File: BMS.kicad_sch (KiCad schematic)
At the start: 89 parts, among them J1 Conn_02x02_Counter_Clockwise, J10 OLED, J2 Conn_02x02_Counter_Clockwise, J3 RJ45, J4 Conn_02x08_Top_Bottom, J5 Conn_02x05_Top_Bottom, J6 Conn_02x02_Counter_Clockwise, J7 Conn_02x02_Counter_Clockwise, J8 Conn_02x08_Top_Bottom, Q1 BSS138LT1G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

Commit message: PCB Improvements - VIAS/Pours UNFINISHED
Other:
- moved on the sheet: BT1, C15, D43, H1, H2, H3, H4, J10, J3, J7, J8, JP1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

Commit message: J5 Bottom Silkscreen, Schematic organise
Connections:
- net Overcurrent_Protection1/V_{OUT} renamed 5V_Out_J4
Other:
- note added: "12v Input Processing"
- note added: "5V Supply"
- note added: "CAN1 ISOLATED (J6)"
- note added: "CAN2 Transceiver (J5)"
- note added: "CAN3 Transceiver (J3)"
- note added: "Connector J1 - Serial ISOLATED"
- note added: "Connector J6 - CAN ISOLATED"
- note added: "RS-485 Transceiver (J7)"
- note added: "Scrap Book"
- note added: "Serial ISOLATED (J1)"
- note added: "UART Buffer (J5)"
- note removed: "CAN Connector ISOLATED"
- note removed: "CAN Transceivers - Non Isolated"
- note removed: "CAN1 ISOLATED"
- note removed: "Power Supply"
- note removed: "RS-485 Interface"
- note removed: "Serial Connector ISOLATED"
- note removed: "Serial ISOLATED"
- note removed: "UART Buffer"
- moved on the sheet: BC1, BC2, BC3, BT1, C11, C12, C13, C14, C15, C16, C17, C18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

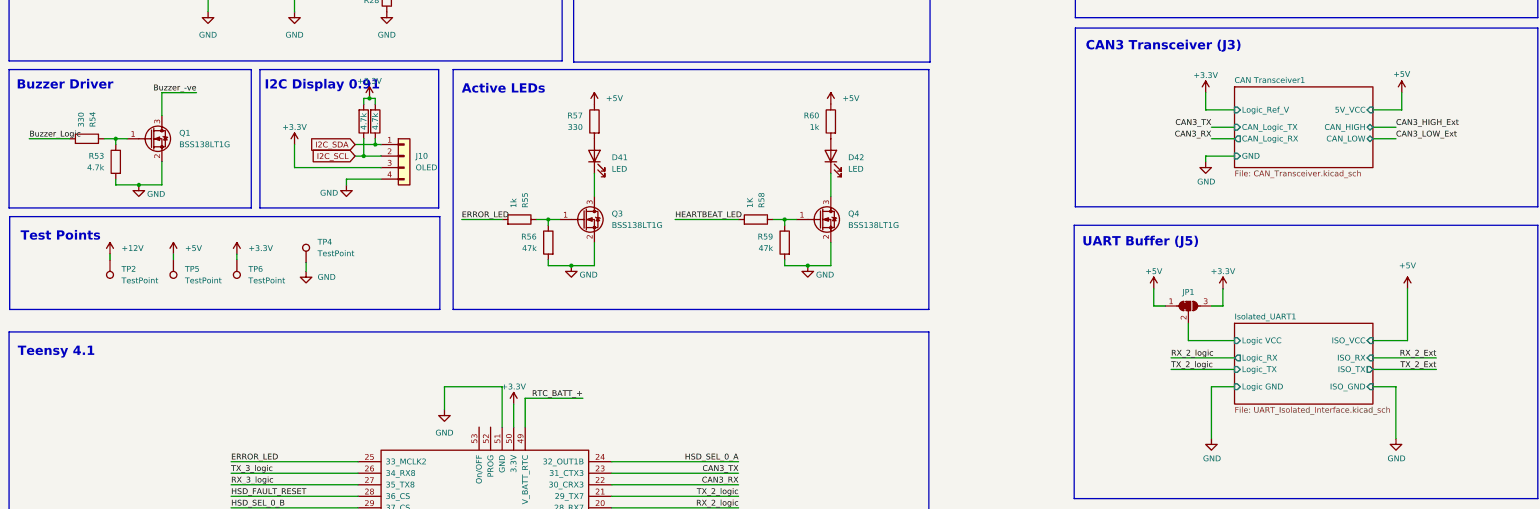
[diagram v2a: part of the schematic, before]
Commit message: Implemented schematic review suggestions (Notes.txt)
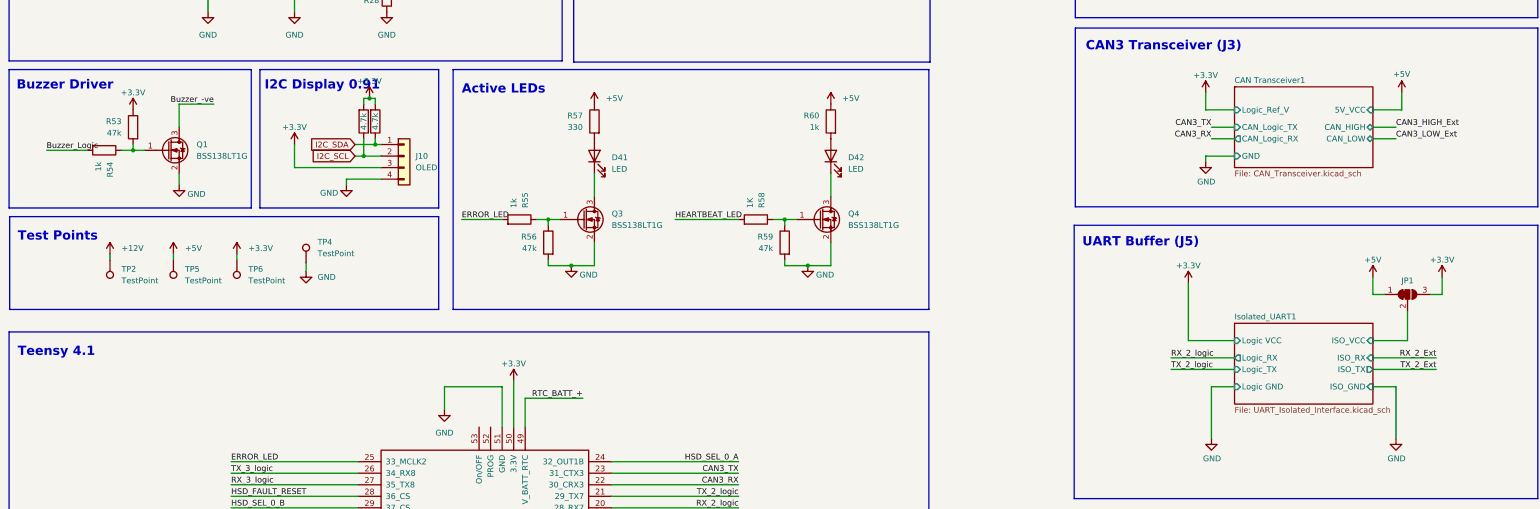
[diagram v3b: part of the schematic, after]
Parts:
- R53: value 4.7k -> 47k
- R54: value 330 -> 1k
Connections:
- net +3.3V: now also R53.1
- net GND: no longer R53.2
- net at Q1.1 (G), R54.1: now also R53.2; no longer R53.1
- net Isolated_UART1/Logic VCC renamed Isolated_UART1/ISO_VCC
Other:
- moved on the sheet: JP1, Q1

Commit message: Added 5V protection capacitors, altered 5V_ISO Output Caps, Corrected RX<>TX for Serial3
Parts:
- removed C13: 470uF, Capacitor_SMD:CP_Elec_10x10, symbol Device:C_Polarized
- added C13, C45, C46: 47uF 16V, Capacitor_SMD:C_1210_3225Metric, symbol Device:C
- C14: value 1uF -> 47uF 16V; footprint Capacitor_SMD:C_0603_1608Metric -> Capacitor_SMD:C_1210_3225Metric; LCSC C15849 -> C5440143
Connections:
- net GND_ISO: now also C13.2, C45.2, C46.2
- net Overcurrent_Protection3/V_{OUT}: now also C13.1, C45.1, C46.1
- net RX_3_logic: now also U3.26 (34_RX8); no longer U3.27 (35_TX8)
- net TX_3_logic: now also U3.27 (35_TX8); no longer U3.26 (34_RX8)

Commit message: Post Chris Layout Review
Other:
- note added: "3V3 Current Draw Teensy: 100mA RS485: 60mA (Max) Digital UART Isolater: 2mA x2 Digital input isolater: 1.5mA x 4 CAN Isolator: 38mA Total 208mA"
- note added: "TODO! LCSC Code is for 220uF. Check Spec and Filter Calcs"
- note added: "TODO! Polarised caps on wrong side of RPP"
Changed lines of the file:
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@@
+		)
+	)
+	(text "3V3 Current Draw\nTeensy: 100mA\nRS485: 60mA (Max)\nDigital UART Isolater: 2mA x2\nDigital input isolater: 1.5mA x 4\nCAN Isolator: 38mA\n\nTotal 208mA"
+		(exclude_from_sim no)
+		(at 611.124 212.598 0)
+		(effects
+			(font
+				(size 2.54 2.54)
+			)
+			(justify left)
 		)
 	)
@@
 		)
 	)
+	(text "TODO! LCSC Code is for 220uF. Check Spec and Filter Calcs"
+		(exclude_from_sim no)
+		(at 73.914 67.818 0)
+		(effects
+			(font
+				(size 1.27 1.27)
+			)
+		)
+	)
 	(text "Hardware License "
 		(exclude_from_sim no)
@@
 		(effects
 			(font
+				(size 1.27 1.27)
+			)
+		)
+	)
+	(text "TODO! Polarised caps on wrong side of RPP"
+		(exclude_from_sim no)
+		(at 62.484 32.004 0)
+		(effects
+			(font

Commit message: Updated RPP Mosfet to 100V device
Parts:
- Q2: LCSC C701057 -> C845605
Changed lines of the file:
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@@
 			)
 		)
-		(property "Datasheet" "https://lcsc.com/datasheet/lcsc_datasheet_2410121656_HUASHUO-HSBA100P03_C701057.pdf"
+		(property "Datasheet" "https://www.lcsc.com/datasheet/C845605.pdf"
 			(at 104.14 57.15 0)
 			(effects
@@
 			)
 		)
-		(property "Description" "P-Ch 30V 100A 2.6mΩ Fast Switching MOSFETs"
+		(property "Description" "100V 100A 4.5mΩ@10V,30A 208W 4V 1 N-Channel PRPAK5x6-8L MOSFETs ROHS"
 			(at 104.14 55.88 0)
 			(effects
@@
 			)
 		)
-		(property "LCSC" "C701057"
+		(property "LCSC" "C845605"
 			(at 104.14 57.15 0)
 			(effects

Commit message: Placed RPP in front of Pi Filter, to protect electrolytics from RP
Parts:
- C1, C2: value 470uF -> 220uF
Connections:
- net +12V: now also C2.1, L1.2; no longer D21.1 (K), Q2.5 (D)
- net +12V_Filtered: no longer names the net of Q2.1 (S), Q2.2 (S), Q2.3 (S)
- net +12V_Filtered: now also D1.1 (K), F1.2; no longer C2.1, L1.2
- net +12V_Fused: no longer names the net of C1.1, L1.1
- net +12V_Fused: now also D21.1 (K), Q2.5 (D); no longer D1.1 (K), F1.2
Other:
- note added: "LPF Pi Filter 10A F_{c}=19.6Hz F_{c}=1/(2*pi*sqrt(F*(C1+C2)))"
- note removed: "LPF Pi Filter 10A F_{c}=87.6Hz"
- note removed: "TODO! LCSC Code is for 220uF. Check Spec and Filter Calcs"
- note removed: "TODO! Polarised caps on wrong side of RPP"
- moved on the sheet: C1, C2, D21, L1, Q2, R28

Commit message: Error LED defaults to ON, driven OFF by Teensy
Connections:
- net +3.3V: now also R56.2
- net GND: no longer R56.2
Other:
- moved on the sheet: R56
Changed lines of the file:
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@@
 	)
 	(junction
-		(at 144.78 125.73)
-		(diameter 0)
-		(color 0 0 0 0)
-	)
-	(junction
 		(at 48.26 100.33)
 		(diameter 0)
@@
 	(wire
 		(pts
-			(xy 144.78 125.73) (xy 149.86 125.73)
-		)
-		(stroke
-			(width 0)
-			(type default)
-		)
-	)
-	(wire
-		(pts
 			(xy 280.67 142.24) (xy 290.83 142.24)
 		)
@@
 	(wire
 		(pts
+			(xy 139.7 110.49) (xy 139.7 115.57)
+		)
+		(stroke
+			(width 0)
+			(type default)
+		)
+	)
+	(wire
+		(pts
 			(xy 69.85 179.07) (xy 97.79 179.07)
 		)
@@
 	(wire
 		(pts
-			(xy 139.7 124.46) (xy 139.7 125.73)
-		)
-		(stroke
-			(width 0)
-			(type default)
-		)
-	)
-	(wire
-		(pts
 			(xy 101.6 97.79) (xy 101.6 99.06)
 		)
@@
 	(wire
 		(pts
+			(xy 139.7 100.33) (xy 139.7 102.87)
+		)
+		(stroke
+			(width 0)
+			(type default)
+		)
+	)
+	(wire
+		(pts
 			(xy 153.67 217.17) (xy 181.61 217.17)
 		)
@@
 	(wire
 		(pts
-			(xy 139.7 116.84) (xy 139.7 115.57)
-		)
-		(stroke
-			(width 0)
-			(type default)
-		)
-	)
-	(wire
-		(pts
 			(xy 459.74 227.33) (xy 466.09 227.33)
 		)
@@
 	(wire
 		(pts
-			(xy 139.7 125.73) (xy 144.78 125.73)
-		)
-		(stroke
-			(width 0)
-			(type default)
-		)
-	)
-	(wire
-		(pts
 			(xy 30.48 349.25) (xy 58.42 349.25)
 		)
@@
 	(symbol
 		(lib_id "Device:R")
-		(at 139.7 120.65 0)
-		(mirror y)
+		(at 139.7 106.68 180)
 		(unit 1)
 		(exclude_from_sim no)
@@
 		(dnp no)
 		(property "Reference" "R56"
-			(at 137.16 119.3799 0)
+			(at 137.16 107.9501 0)
 			(effects
 				(font
@@
 		)
 		(property "Value" "47k"
-			(at 137.16 121.9199 0)
+			(at 137.16 105.4101 0)
 			(effects
 				(font
@@
 		)
 		(property "Footprint" "Resistor_SMD:R_0603_1608Metric"
-			(at 141.478 120.65 90)
+			(at 141.478 106.68 90)
 			(effects
 				(font
@@
 		)
 		(property "Datasheet" "~"
-			(at 139.7 120.65 0)
+			(at 139.7 106.68 0)
 			(effects
 				(font
@@
 		)
 		(property "Description" "Resistor"
-			(at 139.7 120.65 0)
+			(at 139.7 106.68 0)
 			(effects
 				(font
@@
 	)
 	(symbol
+		(lib_id "power:+3.3V")
+		(at 139.7 100.33 0)
+		(unit 1)
+		(exclude_from_sim no)
+		(in_bom yes)
+		(on_board yes)
+		(dnp no)
+		(fields_autoplaced yes)
+		(property "Reference" "#PWR0102"
+			(at 139.7 104.14 0)
+			(effects
+				(font
+					(size 1.27 1.27)
+				)
+				(hide yes)
+			)
+		)
+		(property "Value" "+3.3V"
+			(at 139.7 96.52 0)
+			(effects
+				(font
+					(size 1.27 1.27)
+				)
+			)
+		)
+		(property "Footprint" ""
+			(at 139.7 100.33 0)
+			(effects
+				(font
+					(size 1.27 1.27)
+				)
+				(hide yes)
+			)
+		)
+		(property "Datasheet" ""
+			(at 139.7 100.33 0)
+			(effects
+				(font
+					(size 1.27 1.27)
+				)
+				(hide yes)
+			)
+		)
+		(property "Description" ""
+			(at 139.7 100.33 0)
+			(effects
+				(font
+					(size 1.27 1.27)
+				)
+				(hide yes)
+			)
+		)
+		(pin "1"
+		)
+		(instances
+			(project "BMS"
+				(path "/d7e219ab-f530-45f5-8a23-0e6b6d2e3e0f"
+					(reference "#PWR0102")
+					(unit 1)
+				)
+			)
+		)
+	)
+	(symbol
 		(lib_id "power:GND")
 		(at 85.09 231.14 0)
@@
 	(symbol
 		(lib_id "power:GND")
-		(at 144.78 125.73 0)
+		(at 149.86 125.73 0)
 		(unit 1)
 		(exclude_from_sim no)
@@
 		(dnp no)
 		(property "Reference" "#PWR055"
-			(at 144.78 132.08 0)
+			(at 149.86 132.08 0)
 			(effects
 				(font
@@
 		)
 		(property "Value" "GND"
-			(at 148.59 127.762 0)
+			(at 153.67 127.762 0)
 			(effects
 				(font
@@
 		)
 		(property "Footprint" ""
-			(at 144.78 125.73 0)
+			(at 149.86 125.73 0)
 			(effects
 				(font
@@
 		)
 		(property "Datasheet" ""
-			(at 144.78 125.73 0)
+			(at 149.86 125.73 0)
 			(effects
 				(font
@@
 		)
 		(property "Description" ""
-			(at 144.78 125.73 0)
+			(at 149.86 125.73 0)
 			(effects
 				(font
